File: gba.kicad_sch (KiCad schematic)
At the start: 29 parts, among them IC1 STM32MP157AAB3, IC7 S40FC004C1B2C00000, IC9 NXS0506UPZ, J2 Conn_01x02, J3 MEM2075-00-140-01-A, SW1 SW_MEC_5G, SW2 SW_MEC_5G

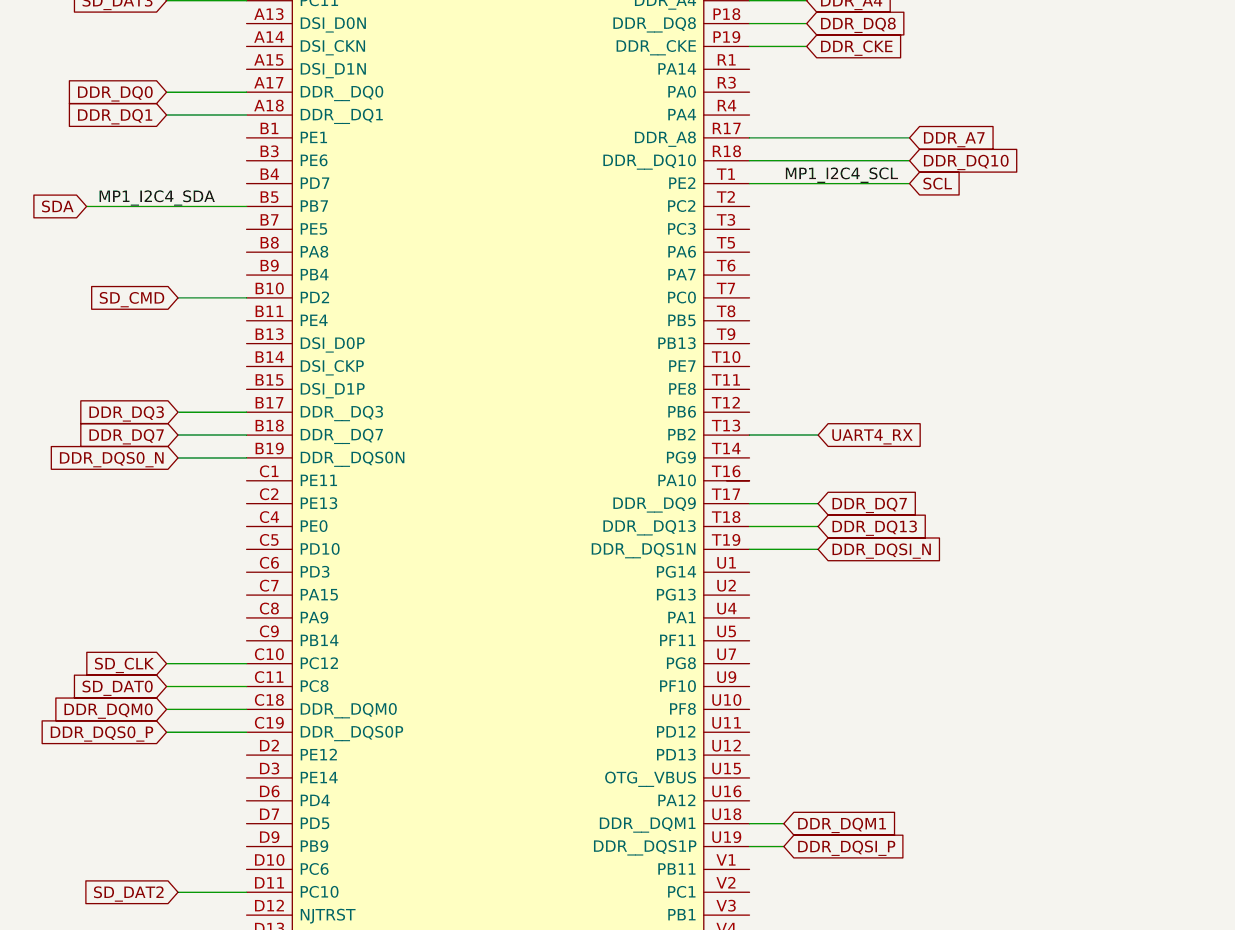
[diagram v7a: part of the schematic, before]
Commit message: Added I2C interface to pmic and stp
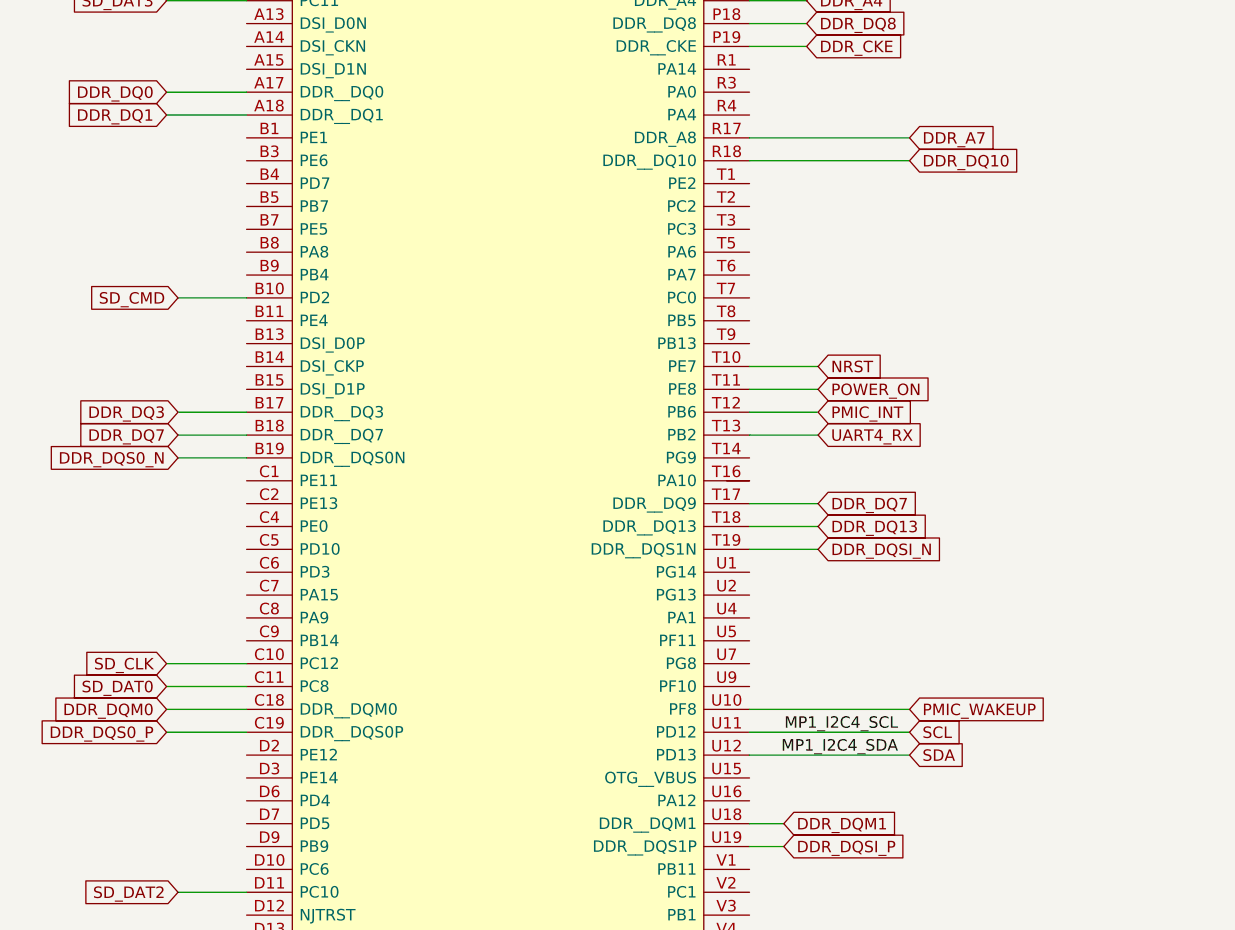
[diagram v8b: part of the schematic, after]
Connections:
- net NRST: now also IC1.T10 (PE7)
- net SCL: now also IC1.U11 (PD12); no longer IC1.T1 (PE2)
- net SDA: now also IC1.U12 (PD13); no longer IC1.B5 (PB7)
- net POWER_ON: now reaches IC1.T11 (PE8)
- net PMIC_INT: now reaches IC1.T12 (PB6)
- net PMIC_WAKEUP: now reaches IC1.U10 (PF8)
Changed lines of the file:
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@@
-    (stroke (width 0) (type default))
-  )
-  (wire (pts (xy 66.04 121.92) (xy 83.82 121.92))
     (stroke (width 0) (type default))
   )
@@
     (stroke (width 0) (type default))
   )
+  (wire (pts (xy 139.7 144.78) (xy 147.32 144.78))
+    (stroke (width 0) (type default))
+  )
   (wire (pts (xy 336.55 125.73) (xy 358.14 125.73))
     (stroke (width 0) (type default))
@@
     (stroke (width 0) (type default))
   )
+  (wire (pts (xy 157.48 182.88) (xy 139.7 182.88))
+    (stroke (width 0) (type default))
+  )
+  (wire (pts (xy 157.48 180.34) (xy 139.7 180.34))
+    (stroke (width 0) (type default))
+  )
   (wire (pts (xy 139.7 38.1) (xy 146.05 38.1))
     (stroke (width 0) (type default))
@@
     (stroke (width 0) (type default))
   )
+  (wire (pts (xy 139.7 139.7) (xy 147.32 139.7))
+    (stroke (width 0) (type default))
+  )
   (wire (pts (xy 77.47 261.62) (xy 83.82 261.62))
     (stroke (width 0) (type default))
@@
     (stroke (width 0) (type default))
   )
+  (wire (pts (xy 139.7 142.24) (xy 147.32 142.24))
+    (stroke (width 0) (type default))
+  )
   (wire (pts (xy 381 49.53) (xy 384.81 49.53))
     (stroke (width 0) (type default))
@@
     (stroke (width 0) (type default))
   )
+  (wire (pts (xy 139.7 177.8) (xy 157.48 177.8))
+    (stroke (width 0) (type default))
+  )
   (wire (pts (xy 255.27 46.99) (xy 259.08 46.99))
     (stroke (width 0) (type default))
@@
   )
   (wire (pts (xy 384.81 52.07) (xy 384.81 54.61))
-    (stroke (width 0) (type default))
-  )
-  (wire (pts (xy 157.48 119.38) (xy 139.7 119.38))
     (stroke (width 0) (type default))
   )
@@
     (effects (font (size 1.27 1.27)) (justify left bottom))
   )
-  (label "MP1_I2C4_SDA" (at 67.31 121.92 0) (fields_autoplaced)
-    (effects (font (size 1.27 1.27)) (justify left bottom))
-  )
-  (label "MP1_I2C4_SCL" (at 156.21 119.38 180) (fields_autoplaced)
+  (label "MP1_I2C4_SCL" (at 156.21 180.34 180) (fields_autoplaced)
     (effects (font (size 1.27 1.27)) (justify right bottom))
   )
+  (label "MP1_I2C4_SDA" (at 156.21 182.88 180) (fields_autoplaced)
+    (effects (font (size 1.27 1.27)) (justify right bottom))
+  )
   (global_label "DDR_ODT" (shape input) (at 77.47 266.7 180) (fields_autoplaced)
     (effects (font (size 1.27 1.27)) (justify right))
@@
     )
   )
+  (global_label "PMIC_INT" (shape input) (at 147.32 144.78 0) (fields_autoplaced)
+    (effects (font (size 1.27 1.27)) (justify left))
+    (property "Intersheetrefs" "${INTERSHEET_REFS}" (at 158.6925 144.78 0)
+      (effects (font (size 1.27 1.27)) (justify left) hide)
+    )
+  )
   (global_label "SD_DAT3" (shape input) (at 295.91 123.19 180) (fields_autoplaced)
     (effects (font (size 1.27 1.27)) (justify right))
@@
     )
   )
+  (global_label "NRST" (shape input) (at 147.32 139.7 0) (fields_autoplaced)
+    (effects (font (size 1.27 1.27)) (justify left))
+    (property "Intersheetrefs" "${INTERSHEET_REFS}" (at 155.0034 139.7 0)
+      (effects (font (size 1.27 1.27)) (justify left) hide)
+    )
+  )
   (global_label "LDO5_2V9" (shape input) (at 394.97 114.3 90) (fields_autoplaced)
     (effects (font (size 1.27 1.27)) (justify left))
@@
     )
   )
-  (global_label "SDA" (shape input) (at 66.04 121.92 180) (fields_autoplaced)
-    (effects (font (size 1.27 1.27)) (justify right))
-    (property "Intersheetrefs" "${INTERSHEET_REFS}" (at 59.5661 121.92 0)
-      (effects (font (size 1.27 1.27)) (justify right) hide)
-    )
-  )
   (global_label "UART4_TX" (shape input) (at 147.32 208.28 0) (fields_autoplaced)
     (effects (font (size 1.27 1.27)) (justify left))
@@
     )
   )
+  (global_label "SDA" (shape input) (at 157.48 182.88 0) (fields_autoplaced)
+    (effects (font (size 1.27 1.27)) (justify left))
+    (property "Intersheetrefs" "${INTERSHEET_REFS}" (at 163.9539 182.88 0)
+      (effects (font (size 1.27 1.27)) (justify left) hide)
+    )
+  )
   (global_label "DDR_A10" (shape input) (at 146.05 76.2 0) (fields_autoplaced)
     (effects (font (size 1.27 1.27)) (justify left))
@@
     )
   )
+  (global_label "SCL" (shape input) (at 157.48 180.34 0) (fields_autoplaced)
+    (effects (font (size 1.27 1.27)) (justify left))
+    (property "Intersheetrefs" "${INTERSHEET_REFS}" (at 163.8934 180.34 0)
+      (effects (font (size 1.27 1.27)) (justify left) hide)
+    )
+  )
   (global_label "DDR_DQ11" (shape input) (at 147.32 231.14 0) (fields_autoplaced)
     (effects (font (size 1.27 1.27)) (justify left))
@@
     )
   )
-  (global_label "SCL" (shape input) (at 157.48 119.38 0) (fields_autoplaced)
-    (effects (font (size 1.27 1.27)) (justify left))
-    (property "Intersheetrefs" "${INTERSHEET_REFS}" (at 163.8934 119.38 0)
+  (global_label "POWER_ON" (shape input) (at 147.32 142.24 0) (fields_autoplaced)
+    (effects (font (size 1.27 1.27)) (justify left))
+    (property "Intersheetrefs" "${INTERSHEET_REFS}" (at 160.3253 142.24 0)
       (effects (font (size 1.27 1.27)) (justify left) hide)
     )
@@
     )
   )
+  (global_label "PMIC_WAKEUP" (shape input) (at 157.48 177.8 0) (fields_autoplaced)
+    (effects (font (size 1.27 1.27)) (justify left))
+    (property "Intersheetrefs" "${INTERSHEET_REFS}" (at 173.5091 177.8 0)
+      (effects (font (size 1.27 1.27)) (justify left) hide)
+    )
+  )
